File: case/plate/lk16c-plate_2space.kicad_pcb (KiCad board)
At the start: 2 copper layers, 76.2 x 76.2 mm, 19 parts

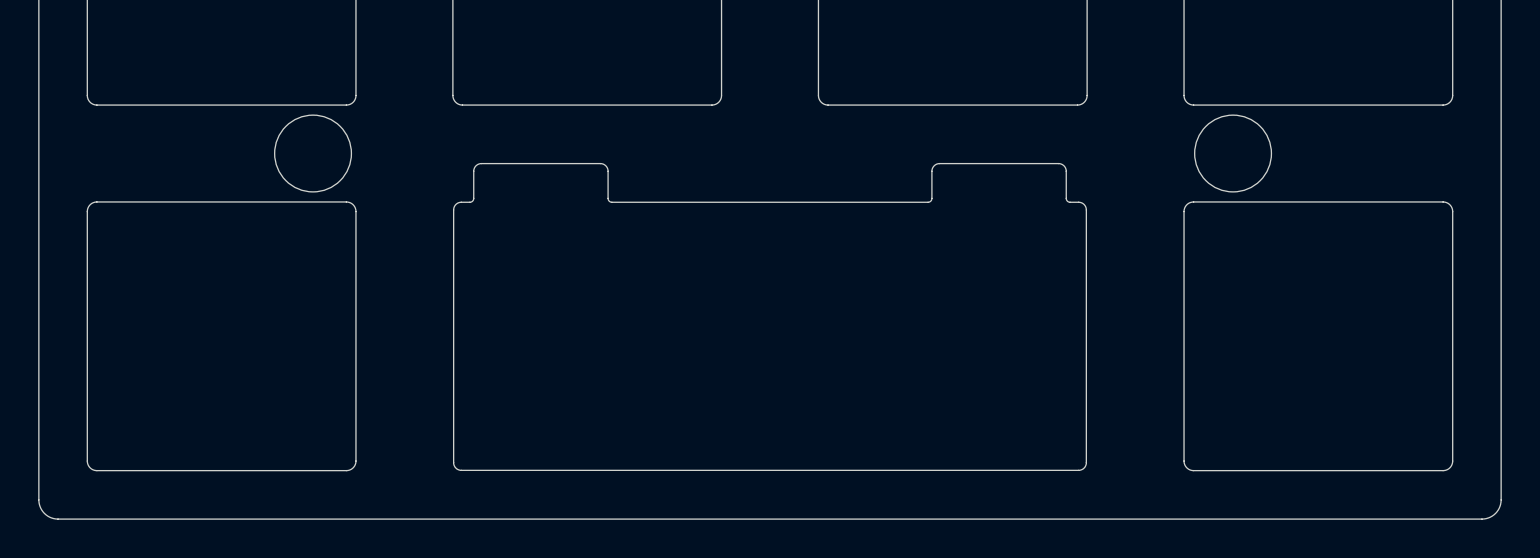
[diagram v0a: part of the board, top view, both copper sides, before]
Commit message: Add ability to use 2× 2U Spacebars as the bottom row (#3)
* Add ability to use 2× 2U Spacebars as the bottom row
* Move Fab DataMatrix footprint
* Add plate variant for 2space
* Fix mounting hole paste
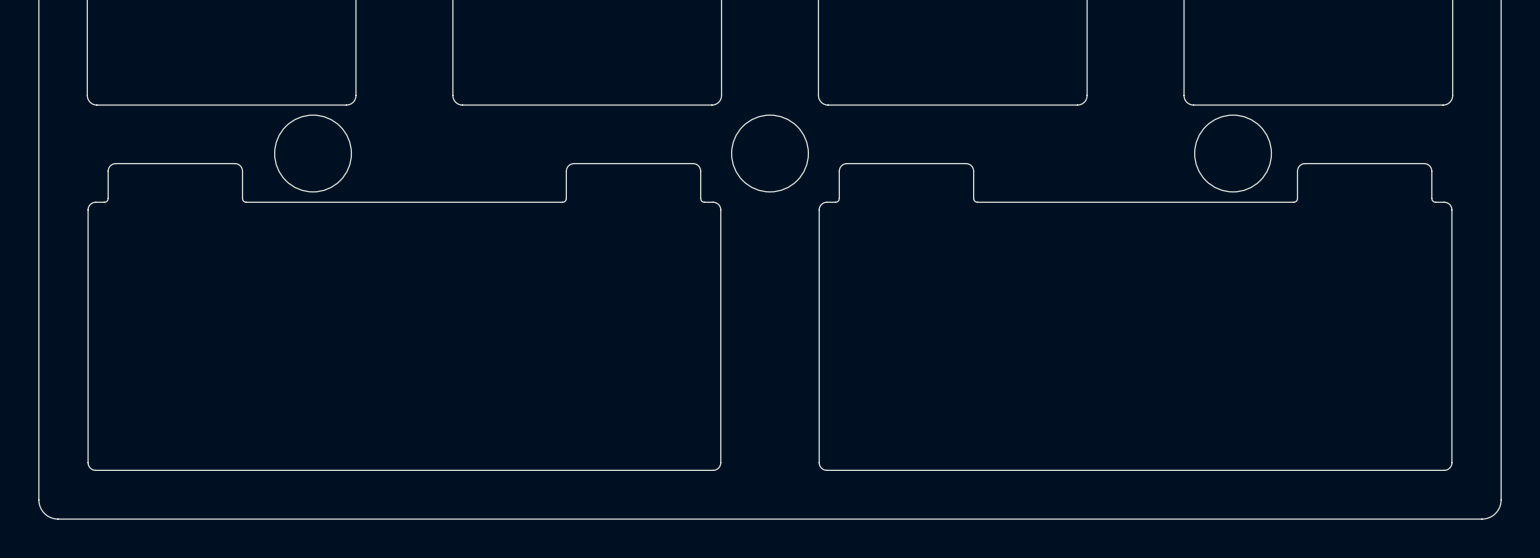
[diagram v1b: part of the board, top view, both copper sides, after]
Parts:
- removed CUT13, CUT17: Plate_MX_1U, LKBD_PlateMX:Plate_MX_1U
- added CUT18: Plate_MX_2U_2x1U, LKBD_PlateMX:Plate_MX_2U_2x1U, F.Cu at (82.5, 92.1)
- added H1: , , F.Cu at (63.5, 82.5)
- moved CUT14 19.0 mm to (44.5, 92.1)
- renumbered CUT15 to CUT14
